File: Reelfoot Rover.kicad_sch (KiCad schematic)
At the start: 2 parts, among them J1 GPIO, U1 7432

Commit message: first complete draft
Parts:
- added C1, C8: 220 uF, symbol Device:C_Polarized
- added C10, C2, C5, C7: 0.1 uF, symbol Device:C
- added C3, C4, C6, C9: 1 uF, symbol Device:C
- added J10: FR Motor, symbol Connector:Conn_01x02_Pin
- added J11: RL Motor, symbol Connector:Conn_01x02_Pin
- added J12: RR Motor, symbol Connector:Conn_01x02_Pin
- added J2: HC-SR04 1, symbol Connector:Conn_01x04_Pin
- added J3: HC-SR04 2, symbol Connector:Conn_01x04_Pin
- added J4: HC-SR04 3, symbol Connector:Conn_01x04_Pin
- added J5: Encoder 1, symbol Connector:Conn_01x03_Pin
- added J6: Encoder 2, symbol Connector:Conn_01x03_Pin
- added J7: Encoder 3, symbol Connector:Conn_01x03_Pin
- added J8: Encoder 4, symbol Connector:Conn_01x03_Pin
- added J9: FL Motor, symbol Connector:Conn_01x02_Pin
- added R1: 330, symbol Device:R
- added R2: 470, symbol Device:R
- added U2, U3: L293D, Package_DIP:DIP-16_W7.62mm, symbol Driver_Motor:L293D
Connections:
- net +3V3: now also C2.1, C3.1, C6.1, C7.1, J5.1 (Pin_1), J6.1 (Pin_1), J7.1 (Pin_1), J8.1 (Pin_1), U2.16 (VCC1), U3.16 (VCC1)
- net +5V: now also C1.1, C8.1, J2.1 (Pin_1), J3.1 (Pin_1), J4.1 (Pin_1)
- net FL Enc: now also J5.3 (Pin_3)
- net FL ML1: now also U2.2 (1A)
- net FL ML2: now also U2.7 (2A)
- net FR Enc: now also J6.3 (Pin_3)
- net FR ML1: now also U3.2 (1A)
- net FR ML2: now also U3.7 (2A)
- net GND: now also U1.10, U1.11, U1.12, U1.13, U1.8, U1.9, C10.2, C2.2, C3.2, C4.2, C5.2, C6.2, C7.2, C9.2, J2.4 (Pin_4), J3.4 (Pin_4), J4.4 (Pin_4), J5.2 (Pin_2), J6.2 (Pin_2), J7.2 (Pin_2), J8.2 (Pin_2), R2.2, U2.12 (GND), U2.13 (GND), U2.4 (GND), U2.5 (GND), U3.12 (GND), U3.13 (GND), U3.4 (GND), U3.5 (GND)
- net M Enable: now also U2.1 (EN1,2), U2.9 (EN3,4), U3.1 (EN1,2), U3.9 (EN3,4)
- net RL Enc: now also J7.3 (Pin_3)
- net RL ML1: now also U2.10 (3A)
- net RL ML2: now also U2.15 (4A)
- net RR Enc: now also J8.3 (Pin_3)
- net RR ML1: now also U3.10 (3A)
- net RR ML2: now also U3.15 (4A)
- net SO Echo: now also R1.2, R2.1
- net SO Trig 1: now also J2.2 (Pin_2)
- net SO Trig 2: now also J3.2 (Pin_2)
- net SO Trig 3: now also J4.2 (Pin_2)
- net SO Echo 1: now reaches U1.1
- net SO Echo 1: now also J2.3 (Pin_3)
- net SO Echo 2: now reaches U1.2
- net SO Echo 2: now also U1.5, J3.3 (Pin_3)
- net at U1.6: now also R1.1
- net GPIO20 renamed GPIO 20
- new net: C1.2, C4.1, C5.1, U2.8 (VCC2)
- new net: C10.1, C8.2, C9.1, U3.8 (VCC2)
- new net FL+: J9.1 (Pin_1), U2.3 (1Y)
- new net FL-: J9.2 (Pin_2), U2.6 (2Y)
- new net FR+: J10.1 (Pin_1), U3.3 (1Y)
- new net FR-: J10.2 (Pin_2), U3.6 (2Y)
- new net RL+: J11.1 (Pin_1), U2.11 (3Y)
- new net RL-: J11.2 (Pin_2), U2.14 (4Y)
- new net RR+: J12.1 (Pin_1), U3.11 (3Y)
- new net RR-: J12.2 (Pin_2), U3.14 (4Y)
- new net SO Echo 3: J4.3 (Pin_3)
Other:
- note added: "Left Motor Driver"
- note added: "Right Motor Driver"
- note added: "Sonar Echo Multiplexing"
- note added: "Unused Or Gates (Grounded)"
- moved on the sheet: J1, U1A, U1B, U1C

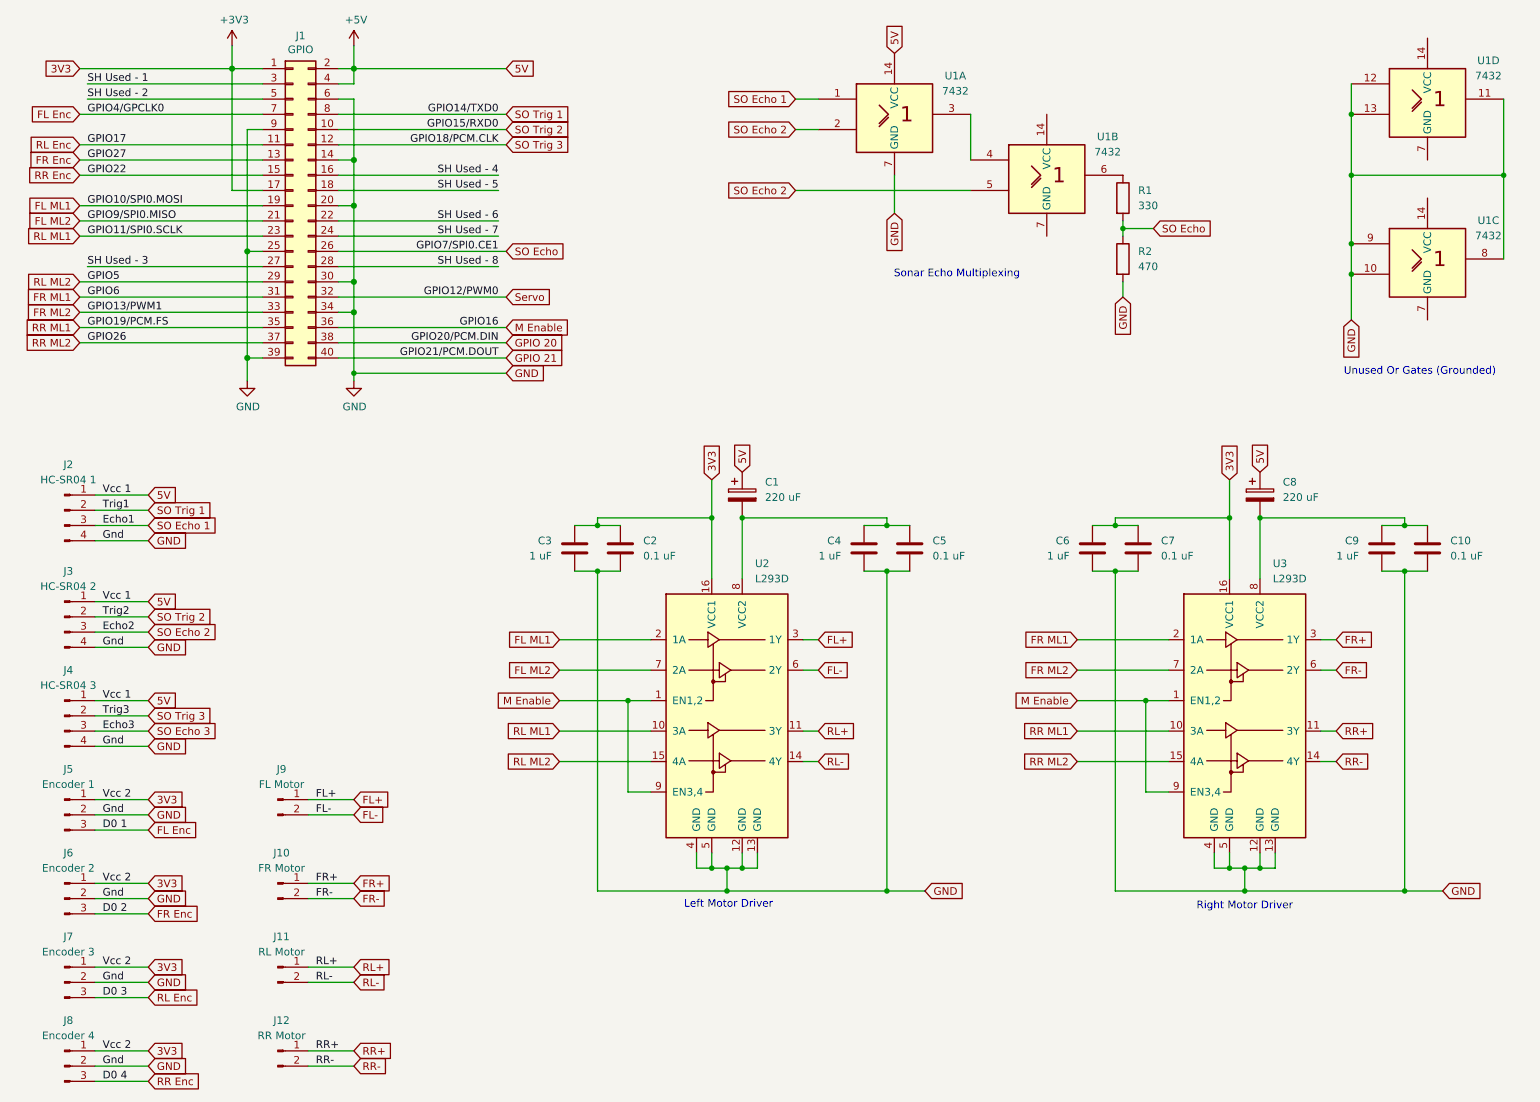
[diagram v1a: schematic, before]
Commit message: Corrected capacitor connections and values.
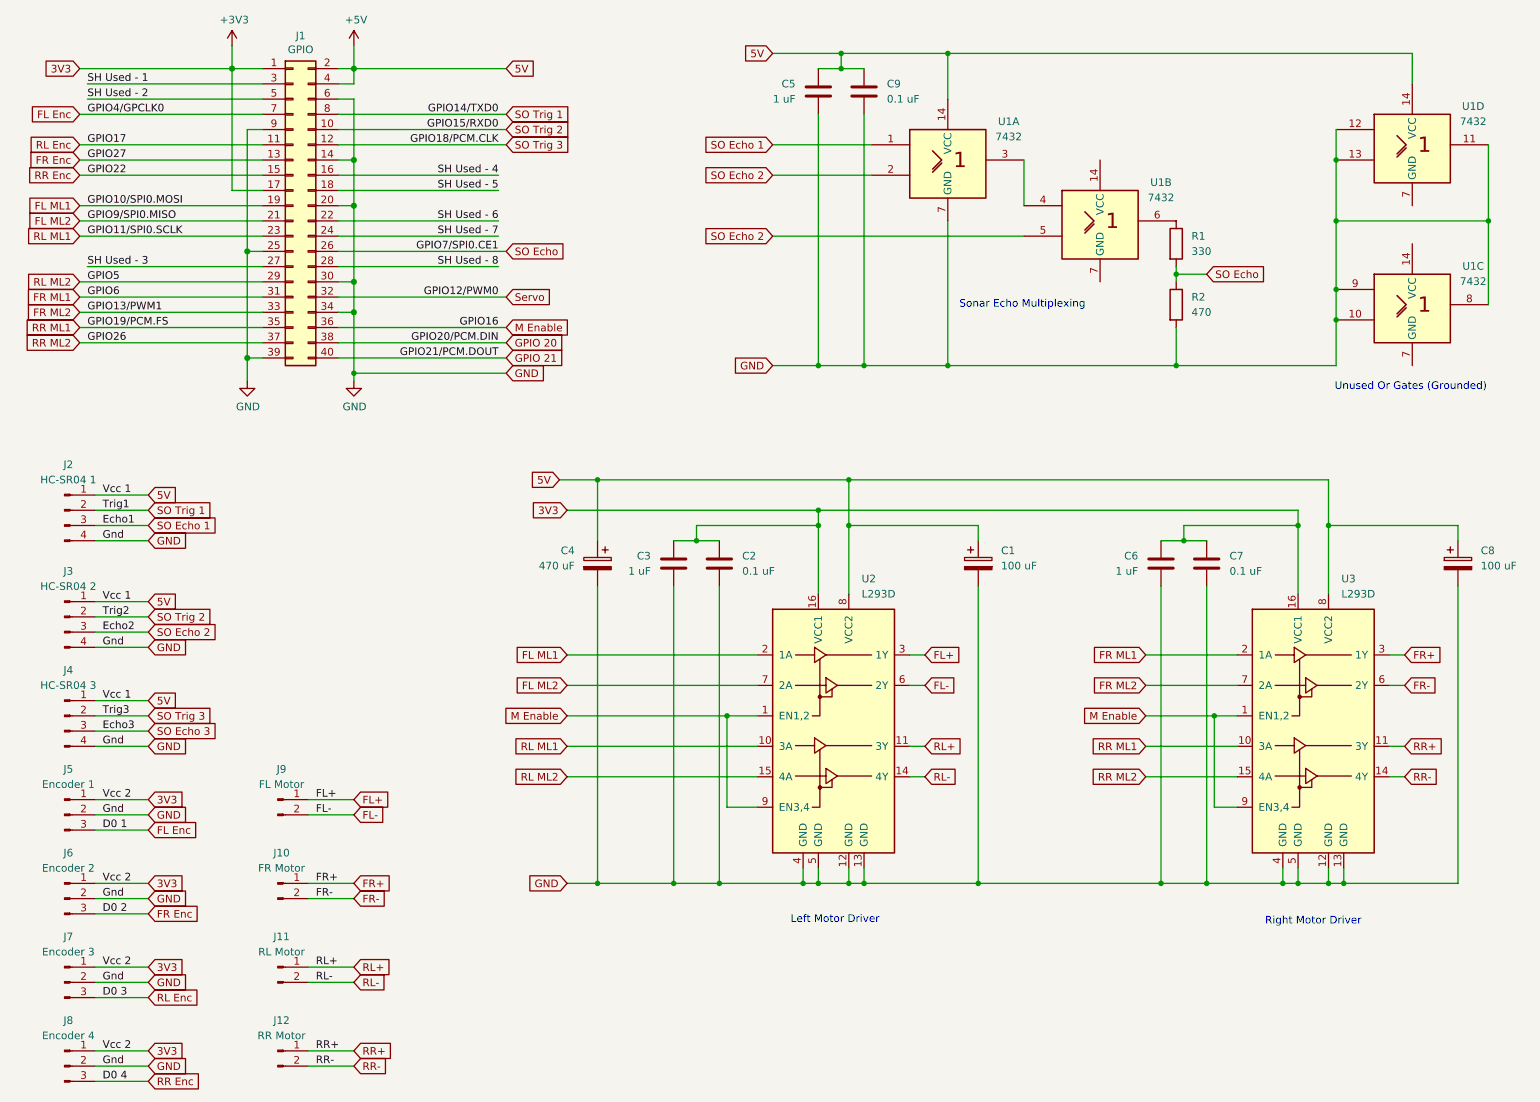
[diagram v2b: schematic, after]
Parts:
- removed C10: 0.1 uF, symbol Device:C
- removed C4: 1 uF, symbol Device:C
- added C4: 470 uF, symbol Device:C_Polarized
- C1, C8: value 220 uF -> 100 uF
- C5: value 0.1 uF -> 1 uF
- C9: value 1 uF -> 0.1 uF
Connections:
- net +5V: now also C5.1, C9.1, U1.14 (VCC), U2.8 (VCC2), U3.8 (VCC2), C4.1
- net GND: now also C1.2, C8.2, C4.2
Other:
- moved on the sheet: C1, C2, C3, C6, C7, C8, R1, R2, U1A, U1B, U1C, U1D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

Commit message: Footprint selection and beginning the PCB layout.
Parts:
- C1, C8: footprint (none) -> Capacitor_THT:CP_Radial_D5.0mm_P2.00mm
- C2, C3, C5, C6, C7, C9: footprint (none) -> Capacitor_THT:C_Disc_D5.0mm_W2.5mm_P5.00mm
- C4: footprint (none) -> Capacitor_THT:CP_Radial_D8.0mm_P2.50mm
- J10, J11, J12, J9: footprint (none) -> Connector_PinHeader_2.54mm:PinHeader_1x02_P2.54mm_Vertical
- J2, J3, J4: footprint (none) -> Connector_PinHeader_2.54mm:PinHeader_1x04_P2.54mm_Vertical
- J5, J6, J7, J8: footprint (none) -> Connector_PinHeader_2.54mm:PinHeader_1x03_P2.54mm_Vertical
- R1, R2: footprint (none) -> Resistor_THT:R_Axial_DIN0207_L6.3mm_D2.5mm_P5.08mm_Vertical
- U1: footprint (none) -> Package_DIP:DIP-14_W7.62mm
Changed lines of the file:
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@@
 			)
 		)
-		(property "Footprint" ""
+		(property "Footprint" "Package_DIP:DIP-14_W7.62mm"
 			(at 247.65 62.23 0)
 			(hide yes)
@@
 			)
 		)
-		(property "Footprint" ""
+		(property "Footprint" "Resistor_THT:R_Axial_DIN0207_L6.3mm_D2.5mm_P5.08mm_Vertical"
 			(at 206.502 62.23 90)
 			(hide yes)
@@
 			)
 		)
-		(property "Footprint" ""
+		(property "Footprint" "Package_DIP:DIP-14_W7.62mm"
 			(at 247.65 35.56 0)
 			(hide yes)
@@
 			)
 		)
-		(property "Footprint" ""
+		(property "Footprint" "Connector_PinHeader_2.54mm:PinHeader_1x02_P2.54mm_Vertical"
 			(at 58.42 172.72 0)
 			(hide yes)
@@
 			)
 		)
-		(property "Footprint" ""
+		(property "Footprint" "Connector_PinHeader_2.54mm:PinHeader_1x02_P2.54mm_Vertical"
 			(at 58.42 158.75 0)
 			(hide yes)
@@
 			)
 		)
-		(property "Footprint" ""
+		(property "Footprint" "Connector_PinHeader_2.54mm:PinHeader_1x04_P2.54mm_Vertical"
 			(at 22.86 96.52 0)
 			(hide yes)
@@
 			)
 		)
-		(property "Footprint" ""
+		(property "Footprint" "Resistor_THT:R_Axial_DIN0207_L6.3mm_D2.5mm_P5.08mm_Vertical"
 			(at 206.502 52.07 90)
 			(hide yes)
@@
 			)
 		)
-		(property "Footprint" ""
+		(property "Footprint" "Connector_PinHeader_2.54mm:PinHeader_1x04_P2.54mm_Vertical"
 			(at 22.86 130.81 0)
 			(hide yes)
@@
 			)
 		)
-		(property "Footprint" ""
+		(property "Footprint" "Capacitor_THT:CP_Radial_D8.0mm_P2.50mm"
 			(at 110.7948 109.22 0)
 			(hide yes)
@@
 			)
 		)
-		(property "Footprint" ""
+		(property "Footprint" "Capacitor_THT:C_Disc_D5.0mm_W2.5mm_P5.00mm"
 			(at 204.7748 109.22 0)
 			(hide yes)
@@
 			)
 		)
-		(property "Footprint" ""
+		(property "Footprint" "Connector_PinHeader_2.54mm:PinHeader_1x03_P2.54mm_Vertical"
 			(at 22.86 189.23 0)
 			(hide yes)
@@
 			)
 		)
-		(property "Footprint" ""
+		(property "Footprint" "Capacitor_THT:CP_Radial_D5.0mm_P2.00mm"
 			(at 256.2352 109.22 0)
 			(hide yes)
@@
 			)
 		)
-		(property "Footprint" ""
+		(property "Footprint" "Package_DIP:DIP-14_W7.62mm"
 			(at 170.18 38.1 0)
 			(hide yes)
@@
 			)
 		)
-		(property "Footprint" ""
+		(property "Footprint" "Package_DIP:DIP-14_W7.62mm"
 			(at 195.58 48.26 0)
 			(hide yes)
@@
 			)
 		)
-		(property "Footprint" ""
+		(property "Footprint" "Capacitor_THT:C_Disc_D5.0mm_W2.5mm_P5.00mm"
 			(at 214.3252 109.22 0)
 			(hide yes)
@@
 			)
 		)
-		(property "Footprint" ""
+		(property "Footprint" "Connector_PinHeader_2.54mm:PinHeader_1x03_P2.54mm_Vertical"
 			(at 22.86 147.32 0)
 			(hide yes)
@@
 			)
 		)
-		(property "Footprint" ""
+		(property "Footprint" "Capacitor_THT:C_Disc_D5.0mm_W2.5mm_P5.00mm"
 			(at 147.6248 30.48 0)
 			(hide yes)
@@
 			)
 		)
-		(property "Footprint" ""
+		(property "Footprint" "Connector_PinHeader_2.54mm:PinHeader_1x03_P2.54mm_Vertical"
 			(at 22.86 175.26 0)
 			(hide yes)
@@
 			)
 		)
-		(property "Footprint" ""
+		(property "Footprint" "Connector_PinHeader_2.54mm:PinHeader_1x04_P2.54mm_Vertical"
 			(at 22.86 114.3 0)
 			(hide yes)
@@
 			)
 		)
-		(property "Footprint" ""
+		(property "Footprint" "Connector_PinHeader_2.54mm:PinHeader_1x02_P2.54mm_Vertical"
 			(at 58.42 186.69 0)
 			(hide yes)
@@
 			)
 		)
-		(property "Footprint" ""
+		(property "Footprint" "Connector_PinHeader_2.54mm:PinHeader_1x03_P2.54mm_Vertical"
 			(at 22.86 161.29 0)
 			(hide yes)
@@
 			)
 		)
-		(property "Footprint" ""
+		(property "Footprint" "Capacitor_THT:C_Disc_D5.0mm_W2.5mm_P5.00mm"
 			(at 157.1752 30.48 0)
 			(hide yes)
@@
 			)
 		)
-		(property "Footprint" ""
+		(property "Footprint" "Connector_PinHeader_2.54mm:PinHeader_1x02_P2.54mm_Vertical"
 			(at 58.42 144.78 0)
 			(hide yes)
@@
 			)
 		)
-		(property "Footprint" ""
+		(property "Footprint" "Capacitor_THT:C_Disc_D5.0mm_W2.5mm_P5.00mm"
 			(at 123.4948 109.22 0)
 			(hide yes)
@@
 			)
 		)
-		(property "Footprint" ""
+		(property "Footprint" "Capacitor_THT:CP_Radial_D5.0mm_P2.00mm"
 			(at 176.2252 109.22 0)
 			(hide yes)
@@
 			)
 		)
-		(property "Footprint" ""
+		(property "Footprint" "Capacitor_THT:C_Disc_D5.0mm_W2.5mm_P5.00mm"
 			(at 133.0452 109.22 0)
 			(hide yes)

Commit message: Placed components, modified resistor footprint
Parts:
- R1, R2: footprint Resistor_THT:R_Axial_DIN0207_L6.3mm_D2.5mm_P5.08mm_Vertical -> Resistor_THT:R_Axial_DIN0207_L6.3mm_D2.5mm_P7.62mm_Horizontal
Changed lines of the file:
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@@
 			)
 		)
-		(property "Footprint" "Resistor_THT:R_Axial_DIN0207_L6.3mm_D2.5mm_P5.08mm_Vertical"
+		(property "Footprint" "Resistor_THT:R_Axial_DIN0207_L6.3mm_D2.5mm_P7.62mm_Horizontal"
 			(at 206.502 62.23 90)
 			(hide yes)
@@
 			)
 		)
-		(property "Footprint" "Resistor_THT:R_Axial_DIN0207_L6.3mm_D2.5mm_P5.08mm_Vertical"
+		(property "Footprint" "Resistor_THT:R_Axial_DIN0207_L6.3mm_D2.5mm_P7.62mm_Horizontal"
 			(at 206.502 52.07 90)
 			(hide yes)

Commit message: Corrected PWM inputs for motors, and updated part numbers to read better.
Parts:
- renumbered C4 to C1, C3 to C2, C2 to C3, C6 to C4, C7 to C5, C5 to C6, C9 to C7, C1 to C8, C8 to C9, U2 to U1, U3 to U2, U1 to U3
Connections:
- net GPIO 20 renamed RR Enable
- net GPIO 21 renamed FR Enable
- net FR Enable: now also U2.1 (EN1,2), U2.9 (EN3,4)
- removed net M Enable: J1.36 (Pin_36), U1.1 (EN1,2), U1.9 (EN3,4), U2.1 (EN1,2), U2.9 (EN3,4)
- net Servo renamed RL Enable
- net RL Enable: now also U1.9 (EN3,4)
- new net FL Enable: J1.36 (Pin_36), U1.1 (EN1,2)

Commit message: Routing more connections
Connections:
- net FR Enable: no longer U2.9 (EN3,4)
- net RR Enable: now also U2.9 (EN3,4)
- net SO Echo 2: no longer U3.5
- net SO Echo 3: now also U3.5
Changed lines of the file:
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@@
 		)
 	)
-	(global_label "FR Enable"
+	(global_label "RR Enable"
 		(shape input)
 		(at 203.2 146.05 180)
@@
 		)
 		(property "Intersheetrefs" "${INTERSHEET_REFS}"
-			(at 190.4437 146.05 0)
+			(at 190.2623 146.05 0)
 			(hide yes)
 			(show_name no)
@@
 		)
 	)
-	(global_label "SO Echo 2"
+	(global_label "SO Echo 3"
 		(shape input)
 		(at 140.97 50.8 180)
